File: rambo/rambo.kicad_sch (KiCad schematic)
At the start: 22 parts, among them Q1 2N7000, SW1 SW_DIP_x04, U1 74LS139, U10 74HCT04, U11 74LS245, U12 74HCT00, U13 74LS85, U14 74HCT02, U15 74HCT02, U16 74LS139, U17 74HCT04, U18 74HCT00, U19 74HCT02, U2 74HCT273, U3 74LS191, U4 74LS191, U5 74LS191, U6 74LS191, U7 74LS191, U8 AS6C4008-55PCN, U9 AS6C4008-55PCN

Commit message: Add card edge connector and power connector
Still missing display LEDS, expansion connector
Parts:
- added J1: Barrel_Jack, symbol Connector:Barrel_Jack
- added J2: Conn_02x25_Odd_Even, symbol Connector_Generic:Conn_02x25_Odd_Even
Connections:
- net +5V: now also J1.1
- net GND: now also J1.2, J2.10 (Pin_10), J2.12 (Pin_12), J2.14 (Pin_14), J2.16 (Pin_16), J2.18 (Pin_18), J2.2 (Pin_2), J2.20 (Pin_20), J2.22 (Pin_22), J2.24 (Pin_24), J2.26 (Pin_26), J2.28 (Pin_28), J2.30 (Pin_30), J2.32 (Pin_32), J2.34 (Pin_34), J2.36 (Pin_36), J2.38 (Pin_38), J2.4 (Pin_4), J2.40 (Pin_40), J2.42 (Pin_42), J2.44 (Pin_44), J2.46 (Pin_46), J2.48 (Pin_48), J2.50 (Pin_50), J2.6 (Pin_6), J2.8 (Pin_8)
- net XA0: now also J2.17 (Pin_17)
- net XA1: now also J2.19 (Pin_19)
- net XA2: now also J2.21 (Pin_21)
- net XA3: now also J2.23 (Pin_23)
- net XA4: now also J2.25 (Pin_25)
- net XA5: now also J2.27 (Pin_27)
- net XA6: now also J2.29 (Pin_29)
- net XA7: now also J2.31 (Pin_31)
- net XD0: now also J2.1 (Pin_1)
- net XD1: now also J2.3 (Pin_3)
- net XD2: now also J2.5 (Pin_5)
- net XD3: now also J2.7 (Pin_7)
- net XD4: now also J2.9 (Pin_9)
- net XD5: now also J2.11 (Pin_11)
- net XD6: now also J2.13 (Pin_13)
- net XD7: now also J2.15 (Pin_15)
- net ~{EXTIOSEL}: now also J2.43 (Pin_43)
- net ~{XIN}: now also J2.33 (Pin_33)
- net ~{XOUT}: now also J2.35 (Pin_35)
- net ~{XRESET}: now also J2.37 (Pin_37)
- no-connect marks 31 -> 35
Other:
- moved on the sheet: U16A, U16B, U16C, U19E, U1C, U8, U9

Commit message: footprints picked, capacitors added, beginning layout
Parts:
- added C1, C10, C11, C12, C13, C14, C15, C2, C3, C4, C5, C6, C7, C8, C9: 100nF, Capacitor_THT:C_Disc_D3.8mm_W2.6mm_P2.50mm, symbol Device:C
- J1: footprint (none) -> Connector_BarrelJack:BarrelJack_GCT_DCJ200-10-A_Horizontal
- J2: footprint (none) -> Connector_PinHeader_2.54mm:PinHeader_2x25_P2.54mm_Vertical
- RN1: value R_Network04 -> 4.7K
- SW1: footprint (none) -> Button_Switch_THT:SW_DIP_SPSTx04_Slide_9.78x12.34mm_W7.62mm_P2.54mm
- U1, U13, U16, U3, U4, U5, U6, U7: footprint (none) -> Package_DIP:DIP-16_W7.62mm
- U10, U12, U14, U15, U17, U18, U19: footprint (none) -> Package_DIP:DIP-14_W7.62mm
- U11, U2: footprint (none) -> Package_DIP:DIP-20_W7.62mm
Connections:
- net +5V: now also C1.1, C10.1, C11.1, C12.1, C13.1, C14.1, C15.1, C2.1, C3.1, C4.1, C5.1, C6.1, C7.1, C8.1, C9.1
- net GND: now also C1.2, C10.2, C11.2, C12.2, C13.2, C14.2, C15.2, C2.2, C3.2, C4.2, C5.2, C6.2, C7.2, C8.2, C9.2
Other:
- moved on the sheet: U16B, U16C, U18C, U18D, U19E, U1C

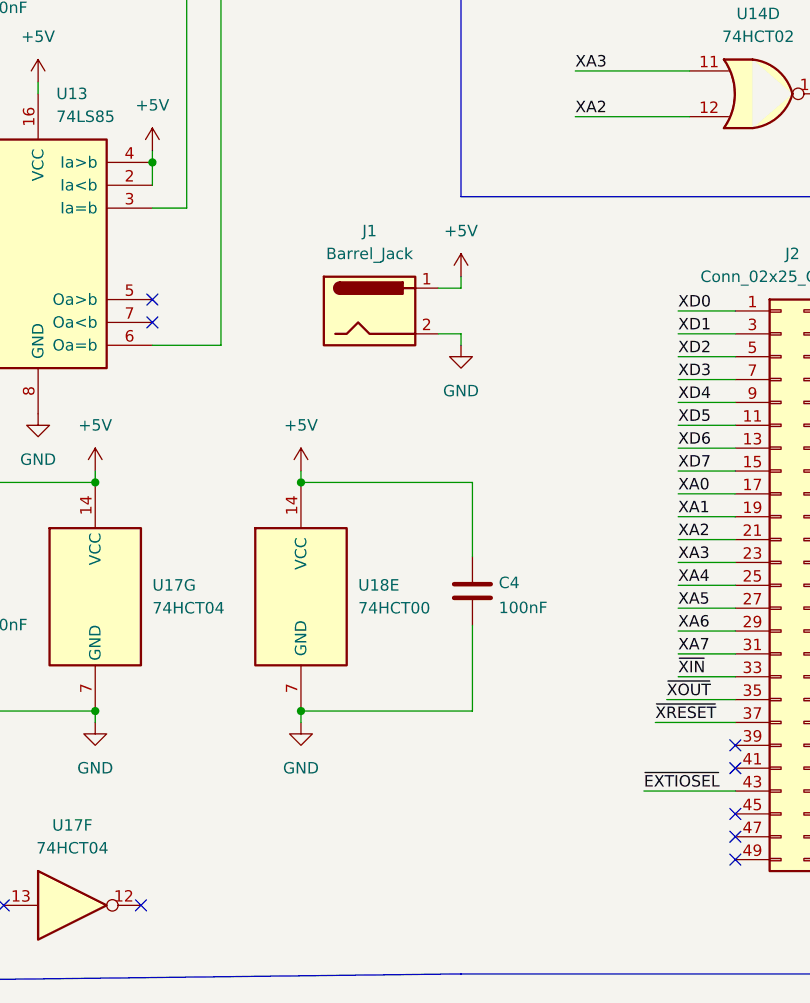
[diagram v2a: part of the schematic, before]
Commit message: added usb b for power
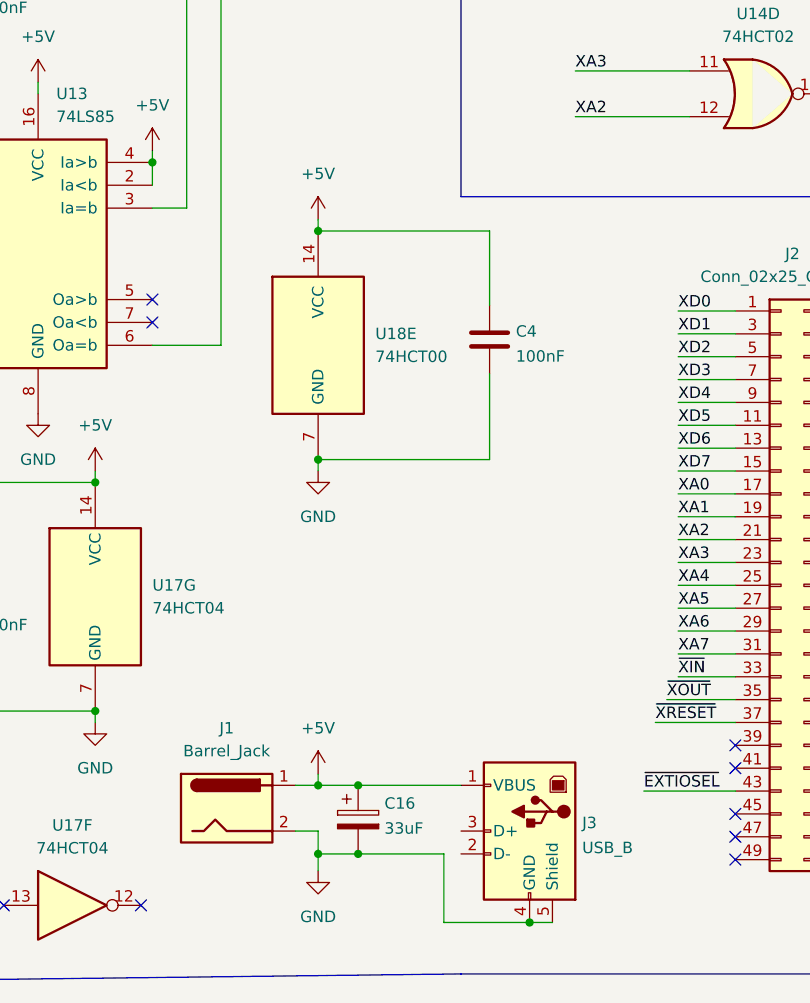
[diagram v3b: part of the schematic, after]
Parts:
- added C16: 33uF, Capacitor_THT:CP_Radial_D6.3mm_P2.50mm, symbol Device:C_Polarized
- added J3: USB_B, Connector_USB:USB_B_OST_USB-B1HSxx_Horizontal, symbol Connector:USB_B
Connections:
- net +5V: now also C16.1, J3.1 (VBUS)
- net GND: now also C16.2, J3.4 (GND), J3.5 (Shield)
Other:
- moved on the sheet: C4, J1, U18E

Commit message: first layout done
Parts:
- removed J1: Barrel_Jack, Connector_BarrelJack:BarrelJack_GCT_DCJ200-10-A_Horizontal, symbol Connector:Barrel_Jack
- removed U15: 74HCT02, Package_DIP:DIP-14_W7.62mm, symbol 74xx:74HCT02
- added J1: Barrel_Jack_Switch, symbol Connector:Barrel_Jack_Switch
- added unit 3 of U14
- renumbered C11 to C1, C2 to C10, C3 to C11, C4 to C12, C1 to C13, C13 to C14, C12 to C15, C5 to C2, C7 to C3, C8 to C4, C10 to C5, C9 to C6, C6 to C7, C14 to C8, C15 to C9, J3 to J2, J2 to J3, U17 to U10, U18 to U12, U19 to U14, U16 to U15
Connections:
- net ADR20 is gone; now on net AR20: U2.12 (Q4)
- net +5V: now also J1.1
- net ACLK: now also U14.1
- net EXTRAADDR: now also U14.4; no longer U14.13
- net GND: now also SW1.5, SW1.6, SW1.7, SW1.8, J1.2, J1.3; no longer SW1.1, SW1.2, SW1.3, SW1.4
- net XA2: now also U14.6; no longer U14.12
- net XA3: now also U14.5; no longer U14.11
- net ~{CKASITRD}: now also U14.12; no longer U14.3
- net ~{CKASITWR}: now also U14.9; no longer U14.6
- net ~{RAMRD}: now also U14.11; no longer U14.2
- net ~{RAMWR}: now also U14.8; no longer U14.5
- net ~{READ}: now also U12.6; no longer U12.3
- net ~{WRITE}: now also U12.3; no longer U12.6
- net at U10.4: now also U12.1; no longer U12.4
- net at RN1.5 (R4), U13.9 (B0): now also SW1.4; no longer SW1.5
- net at RN1.4 (R3), U13.11 (B1): now also SW1.3; no longer SW1.6
- net at RN1.3 (R2), U13.14 (B2): now also SW1.2; no longer SW1.7
- net at RN1.2 (R1), U13.1 (B3): now also SW1.1; no longer SW1.8
- net at U10.2: now also U12.4; no longer U12.1
- new net: U14.13, U14.2
- new net: U14.10, U14.3
- no-connect marks 35 -> 39

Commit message: fixed erc and drc
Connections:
- no-connect marks 39 -> 43
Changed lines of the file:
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@@
   (no_connect (at 167.64 52.07))
   (no_connect (at 167.64 57.15))
+  (no_connect (at 373.38 170.18))
+  (no_connect (at 373.38 172.72))
+  (no_connect (at 124.46 245.745))
+  (no_connect (at 124.46 248.285))
   (no_connect (at 318.77 191.77))
   (no_connect (at 344.17 191.77))

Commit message: inverted select fix
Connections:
- net at U12.2, U12.5, U13.6 (Oa=b): now also U10.9; no longer U11.19 (CE)
- net at U10.8: now also U11.19 (CE)
- no-connect marks 43 -> 41
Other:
- note added: "High Mem"
- note added: "Low Mem"
- note added: "added inverter, per testing note"
- moved on the sheet: U10D
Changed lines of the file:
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@@
   (junction (at 30.48 176.53) (diameter 0) (color 0 0 0 0)
   )
+  (junction (at 30.48 127) (diameter 0) (color 0 0 0 0)
+  )
   (junction (at 90.17 171.45) (diameter 0) (color 0 0 0 0)
   )
@@
   (junction (at 113.03 240.665) (diameter 0) (color 0 0 0 0)
   )
-  (junction (at 30.48 127) (diameter 0) (color 0 0 0 0)
-  )
   (junction (at 167.64 223.52) (diameter 0) (color 0 0 0 0)
   )
@@
   (no_connect (at 21.59 207.645))
   (no_connect (at 36.83 205.105))
-  (no_connect (at 41.91 254))
   (no_connect (at 50.8 254))
-  (no_connect (at 26.67 254))
   (no_connect (at 66.04 254))
   (no_connect (at 73.66 254))
@@
     (stroke (width 0) (type default) (color 0 0 0 0))
   )
-  (wire (pts (xy 30.48 140.97) (xy 30.48 127))
-    (stroke (width 0) (type default) (color 0 0 0 0))
-  )
   (wire (pts (xy 48.26 109.22) (xy 54.61 109.22))
     (stroke (width 0) (type default) (color 0 0 0 0))
@@
     (stroke (width 0) (type default) (color 0 0 0 0))
   )
-  (wire (pts (xy 54.61 127) (xy 30.48 127))
-    (stroke (width 0) (type default) (color 0 0 0 0))
-  )
   (wire (pts (xy 62.23 96.52) (xy 64.77 96.52))
     (stroke (width 0) (type default) (color 0 0 0 0))
@@
     (stroke (width 0) (type default) (color 0 0 0 0))
   )
+  (wire (pts (xy 30.48 127) (xy 30.48 140.97))
+    (stroke (width 0) (type default) (color 0 0 0 0))
+  )
   (wire (pts (xy 148.59 187.96) (xy 154.94 187.96))
     (stroke (width 0) (type default) (color 0 0 0 0))
@@
     (stroke (width 0) (type default) (color 0 0 0 0))
   )
+  (wire (pts (xy 48.895 127) (xy 54.61 127))
+    (stroke (width 0) (type default) (color 0 0 0 0))
+  )
   (wire (pts (xy 342.9 71.12) (xy 349.25 71.12))
     (stroke (width 0) (type default) (color 0 0 0 0))
@@
     (stroke (width 0) (type default) (color 0 0 0 0))
   )
+  (wire (pts (xy 30.48 127) (xy 33.655 127))
+    (stroke (width 0) (type default) (color 0 0 0 0))
+  )
   (wire (pts (xy 137.16 111.76) (xy 142.24 111.76))
     (stroke (width 0) (type default) (color 0 0 0 0))
@@
     (stroke (width 0) (type default) (color 0 0 0 0))
   )
+  (text "added inverter, per testing note" (at 23.495 133.985 0)
+    (effects (font (size 1.27 1.27)) (justify left bottom))
+  )
+  (text "Low Mem" (at 358.14 116.84 0)
+    (effects (font (size 1.27 1.27)) (justify left bottom))
+  )
+  (text "High Mem" (at 358.14 50.8 0)
+    (effects (font (size 1.27 1.27)) (justify left bottom))
+  )
   (label "AR18" (at 342.9 140.97 0)
     (effects (font (size 1.27 1.27)) (justify left bottom))
@@
     (pin "9")
   )
-  (symbol (lib_id "74xx:74HCT04") (at 34.29 254 0) (unit 4)
+  (symbol (lib_id "74xx:74HCT04") (at 41.275 127 0) (unit 4)
     (in_bom yes) (on_board yes) (fields_autoplaced)
-    (property "Reference" "U10" (id 0) (at 34.29 246.2235 0))
-    (property "Value" "74HCT04" (id 1) (at 34.29 248.9986 0))
-    (property "Footprint" "Package_DIP:DIP-14_W7.62mm" (id 2) (at 34.29 254 0)
+    (property "Reference" "U10" (id 0) (at 41.275 119.2235 0))
+    (property "Value" "74HCT04" (id 1) (at 41.275 121.9986 0))
+    (property "Footprint" "Package_DIP:DIP-14_W7.62mm" (id 2) (at 41.275 127 0)
       (effects (font (size 1.27 1.27)) hide)
     )
-    (property "Datasheet" "https://assets.nexperia.com/documents/data-sheet/74HC_HCT04.pdf" (id 3) (at 34.29 254 0)
+    (property "Datasheet" "https://assets.nexperia.com/documents/data-sheet/74HC_HCT04.pdf" (id 3) (at 41.275 127 0)
       (effects (font (size 1.27 1.27)) hide)
     )
